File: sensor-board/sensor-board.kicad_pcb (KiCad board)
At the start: 4 copper layers, 23.4 x 85.9 mm, 104 parts, among them J1 USB_C_Receptacle_USB2.0_16P, J10 cap3, J11 cap4, J2 Conn_01x06, J3 aux pwr, J4 SWD, J5 water 1, J6 water 2, J7 relay, J8 cap1, J9 cap2, K1 SIL03-1A72-71D, Q1 Si2312, Q2 Si2312, SW1 SW_Push, U1 MLPF-WB55-01E3, U10 EKMB130711, U11 DRV5032, U2 STM32WB55CCUx, U3 MCP1703Ax-300xxTT, U4 SHT40-AD1F-R2, U5 VL53L1CXV0FY1, U6 TLV4082, U7 CLS16D24-44, U8 LIS2DE12TR, U9 FDC2114RGHR, Y1 32MHz, Y2 32.768KHz

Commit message: Make cap silkscreen zero-indexed
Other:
- board text added: "cap0"
- board text removed: "cap4"
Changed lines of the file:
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@@
 		)
 	)
-	(gr_text "cap1"
+	(gr_text "cap0"
 		(at 186.69 67.564 0)
 		(layer "F.SilkS")
@@
 		)
 	)
-	(gr_text "cap2\n"
+	(gr_text "cap1"
 		(at 186.69 81.026 0)
 		(layer "F.SilkS")
@@
 		)
 	)
-	(gr_text "cap4\n"
+	(gr_text "cap3"
 		(at 168.4 82.2 90)
 		(layer "F.SilkS")
@@
 		)
 	)
-	(gr_text "cap3\n"
+	(gr_text "cap2"
 		(at 181.864 82.296 90)
 		(layer "F.SilkS")
@@
 		)
 	)
-	(group ""
-		(members "6598a2cd-6cee-47fa-a692-5af72ad08215" "c38db361-1385-4d0e-83ac-f1940c2aaa71")
-	)
 	(embedded_fonts no)

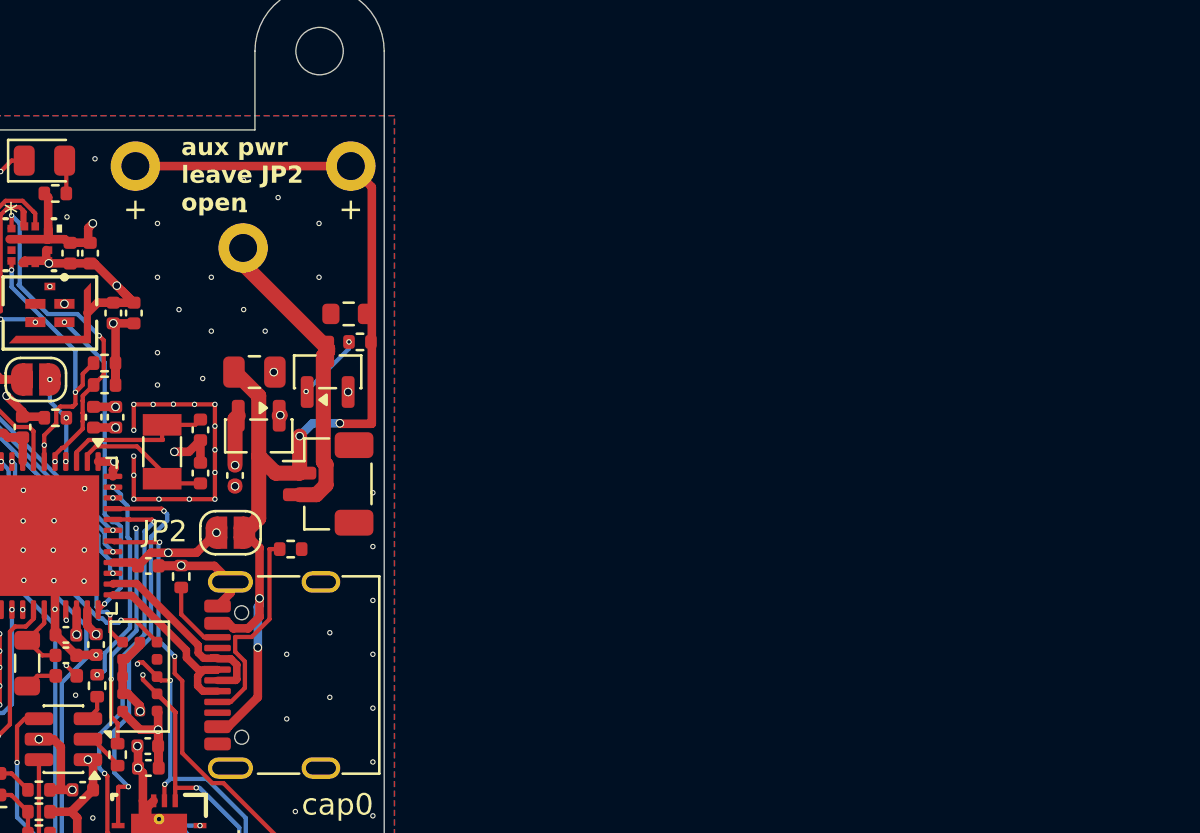
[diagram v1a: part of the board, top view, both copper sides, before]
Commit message: [wip] new power supply circuits
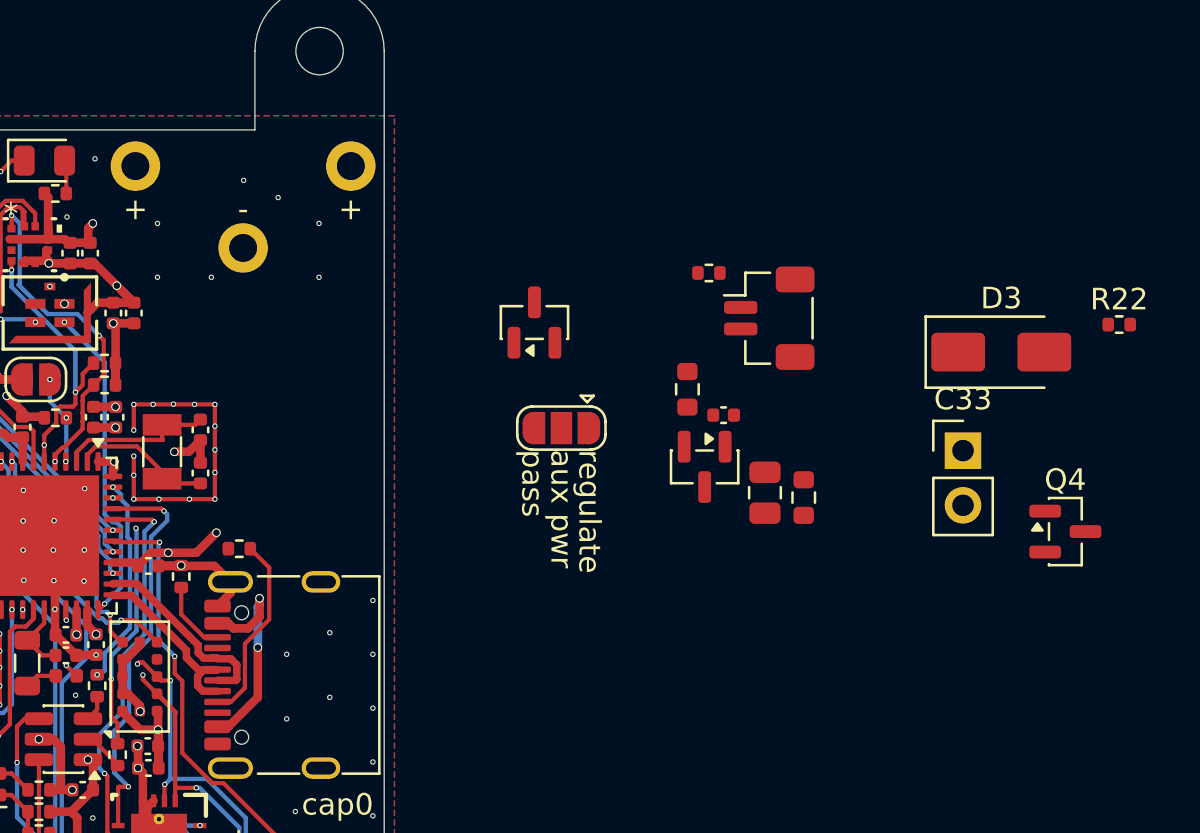
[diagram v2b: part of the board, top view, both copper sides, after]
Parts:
- added C33: 180m, Connector_PinHeader_2.54mm:PinHeader_1x02_P2.54mm_Vertical, F.Cu at (217.4, 50.5)
- added D3: SM4007PL, Diode_SMD:D_SMA, F.Cu at (219.2, 46.0)
- added Q4: Si2312, Package_TO_SOT_SMD:SOT-23, F.Cu at (222.1, 54.3)
- added R22: 1.0k, Resistor_SMD:R_0402_1005Metric, F.Cu at (224.6, 44.7)
- added R23: 2.2M, Resistor_SMD:R_0603_1608Metric, F.Cu at (210.0, 52.7)
- JP2: value USB bypass -> SolderJumper_3_Open; footprint Jumper:SolderJumper-2_P1.3mm_Open_RoundedPad1.0x1.5mm -> Jumper:SolderJumper-3_P1.3mm_Open_RoundedPad1.0x1.5mm
- moved C11 24.4 mm to (208.2, 52.5), turned to -90 degrees
- moved C13 22.9 mm to (206.3, 48.9), turned to 0 degrees
- moved J3 21.9 mm to (208.4, 44.4)
- moved U3 20.7 mm to (205.4, 51.3)
- moved R19 16.5 mm to (205.6, 42.3)
- moved JP2 16.1 mm to (198.8, 49.5)
- moved R18 16.1 mm to (204.6, 47.7), turned to -90 degrees
- moved Q1 9.87 mm to (197.5, 44.6)
- moved R4 2.38 mm to (183.8, 55.1), turned to 180 degrees
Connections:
- net Net-(BT1--) renamed GNDPWR
- BT1 pad 1: Net-(BT1-+) -> +3V0
- C11 pad 1: Net-(BT1-+) -> Net-(D3-K)
- C13 pad 1: +3V0 -> Net-(Q4-S)
- J1 pad A4: Net-(BT1-+) -> VBUS
- J1 pad A9: Net-(BT1-+) -> VBUS
- J1 pad B4: Net-(BT1-+) -> VBUS
- J1 pad B9: Net-(BT1-+) -> VBUS
- J3 pad 1: Net-(BT1-+) -> Net-(J3-Pin_1)
- JP2 pad 1: Net-(BT1-+) -> Net-(D3-K)
- JP2 pad 2: +3V0 -> Net-(J3-Pin_1)
- R18 pad 1: Net-(BT1-+) -> +3V0
- R19 pad 2: Net-(BT1-+) -> +3V0
- U3 pad 2: +3V0 -> Net-(Q4-S)
- U3 pad 3: Net-(BT1-+) -> Net-(D3-K)
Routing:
- net Net-(BT1-+): track 51.7 -> 0.00 mm, vias 4 -> 0
- net GNDPWR: track 14.2 -> 0.00 mm
- net VBUS: track 0.00 -> 10.2 mm, vias 0 -> 2
- net Net-(Q1-G): track 3.18 -> 0.00 mm, vias 2 -> 0
- net +3V0: track 80.0 -> 77.5 mm, vias 22 -> 21
- net Net-(J1-CC1): track 9.75 -> 8.83 mm
- net GND: track 79.5 -> 79.4 mm, vias 195 -> 182
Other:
- board text added: "aux pwr"
- board text added: "pass"
- board text added: "regulate"
- board text removed: "aux pwr leave JP2 open"
